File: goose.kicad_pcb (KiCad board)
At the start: 2 copper layers, 28 x 28 mm, 9 parts, among them J1 Conn_01x04, U1 AT42QT1011-TSHR

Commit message: Update readme and goose_R library symbol
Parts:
- R1: footprint Resistor_SMD:R_0805_2012Metric_Pad1.15x1.40mm_HandSolder -> Resistor_SMD:R_0805_2012Metric
- turned R1 to 0 degrees
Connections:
- C3 pad 1: horrible_goose -> Net-(C3-Pad1)
- R1 pad 1: horrible_goose -> Net-(C2-Pad1)
- R1 pad 2: Net-(C2-Pad1) -> Net-(C3-Pad1)
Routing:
- net horrible_goose: track 8.28 -> 0.00 mm, vias 1 -> 0
- net Net-(C3-Pad1): track 0.00 -> 8.28 mm, vias 0 -> 1

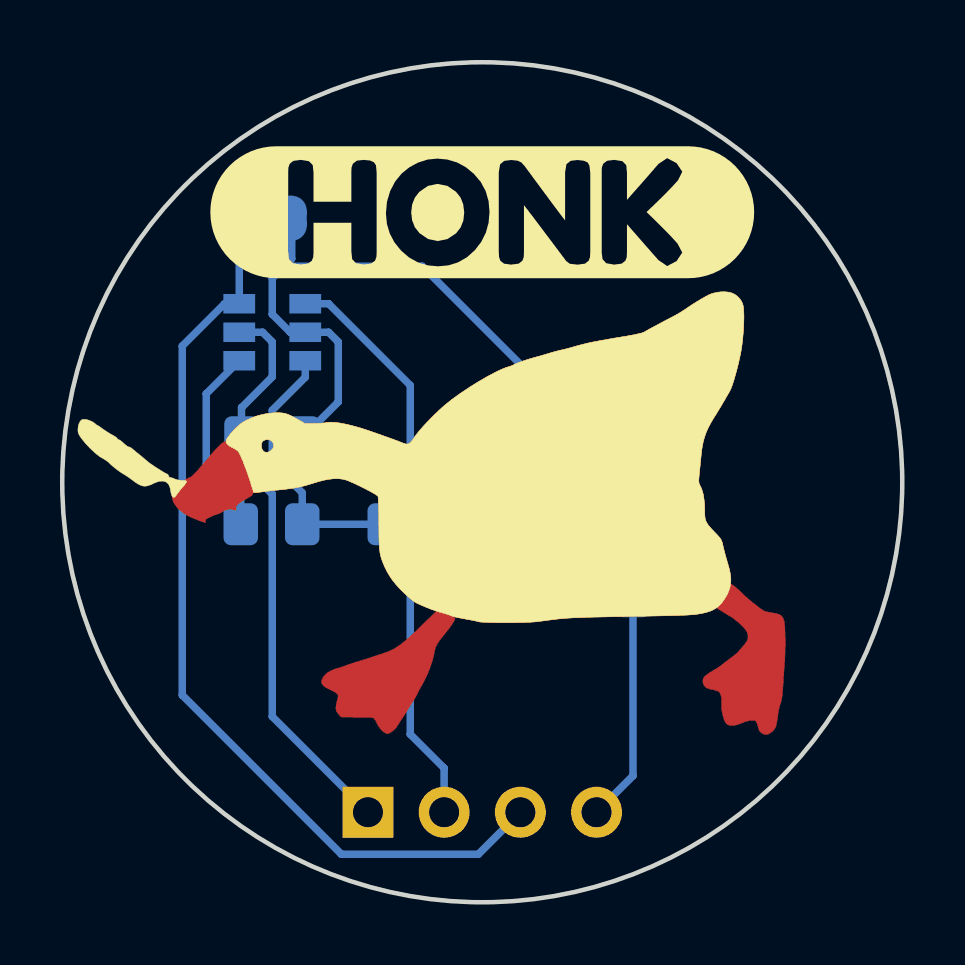
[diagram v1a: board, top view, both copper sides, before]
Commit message: Changed to SAO connector
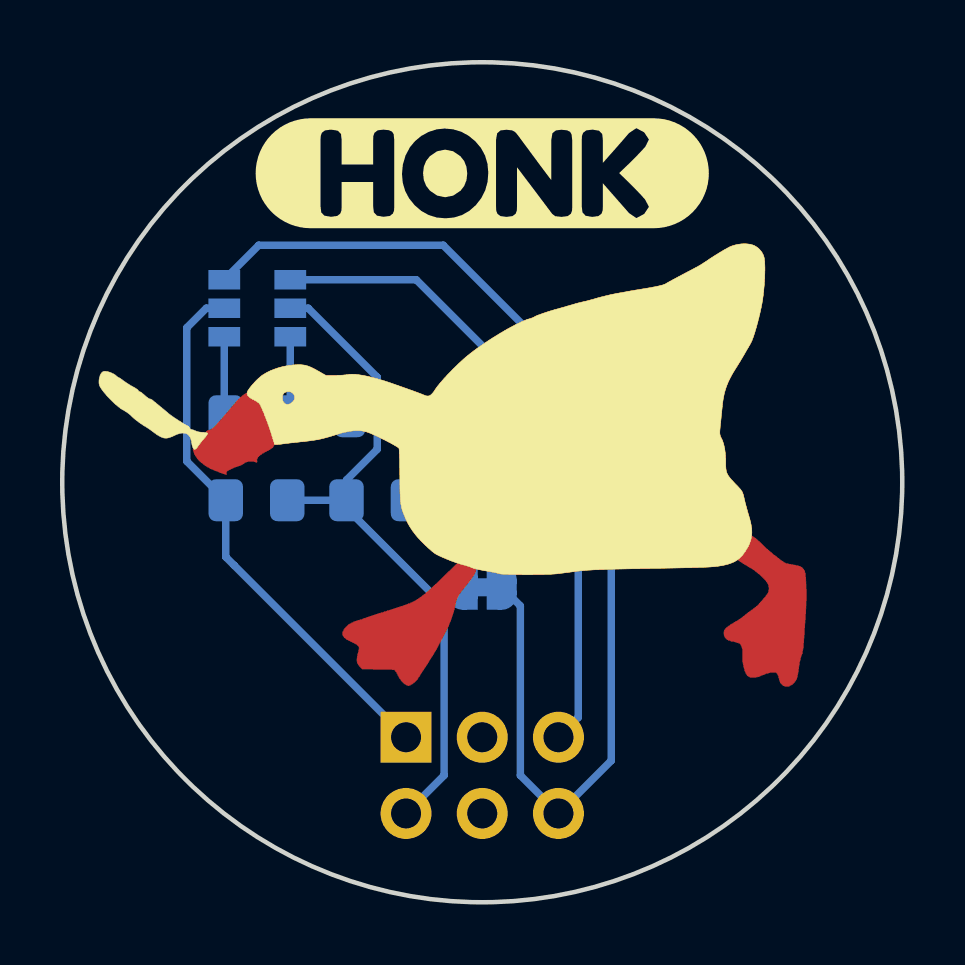
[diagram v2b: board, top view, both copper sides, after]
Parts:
- C3: value 5-20 pF -> 10 pF
- J1: value Conn_01x04 -> SAO Connector; footprint Connector_PinHeader_2.54mm:PinHeader_1x04_P2.54mm_Vertical -> Connector_PinHeader_2.54mm:PinHeader_2x03_P2.54mm_Vertical
- moved JP1 14.2 mm to (100.0, 103.5), turned to 0 degrees
- moved C3 8.15 mm to (96.5, 100.6), turned to 180 degrees
- moved R1 3.76 mm to (96.5, 97.8)
- moved C2 3.63 mm to (92.5, 97.8)
- moved J1 2.80 mm to (97.5, 108.5)
- moved C1 2.16 mm to (92.5, 100.6)
- moved GOOSE1 1.75 mm to (103.7, 99.4)
- moved svg2mod 1.30 mm to (100.0, 89.7)
- moved U1 0.94 mm to (92.5, 94.2)
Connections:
- J1 pad 2: honk -> 0V
- J1 pad 3: sync -> (no net)
- J1 pad 4: 0V -> (no net)
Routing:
- net 0V: track 35.9 -> 23.5 mm
- net sync: track 31.2 -> 38.1 mm
- net Net-(C2-Pad1): track 8.99 -> 4.78 mm
- net Net-(C2-Pad2): track 6.48 -> 2.67 mm
- net honk: track 19.3 -> 22.0 mm
- net Vin: track 19.1 -> 18.2 mm
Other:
- board text added: "*AT42QT101x"
- board text added: "0.1μF"
- board text added: "10nF"
- board text added: "10pF"
- board text added: "1kΩ"
- board text added: "@"
- board text added: "Be Gay Do Crime PCB by heyspacebuck Goose icon by Gnarflordius Untitled Goose Game by House House www.goose.game"
- board text added: "U1*"
- board text removed: "Be Gay Do Crime PCB by @heyspacebuck Goose icon by @Gnarflordius Untitled Goose Game by House House www.goose.game"

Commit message: Goose After Dark
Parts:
- GOOSE1: value Goose -> LOGO; footprint goose:honk_captouch_scaled -> goose:honk_captouch_scaled_afterdark
- moved GOOSE1 5.38 mm to (98.3, 99.4)
